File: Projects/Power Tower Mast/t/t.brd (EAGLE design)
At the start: 16.6 x 21.5 mm, 27 parts

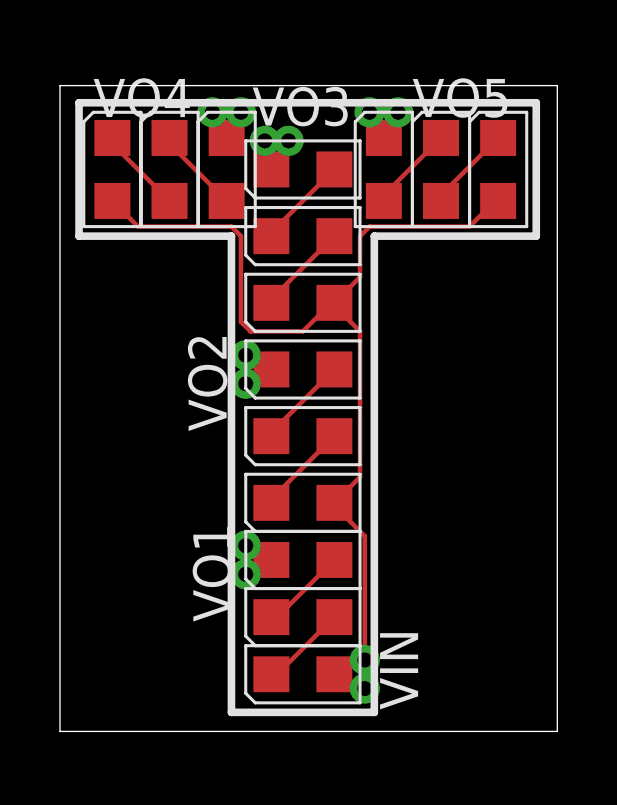
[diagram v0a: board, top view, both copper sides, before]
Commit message: fixed ratio for all letters; continued to update layouts
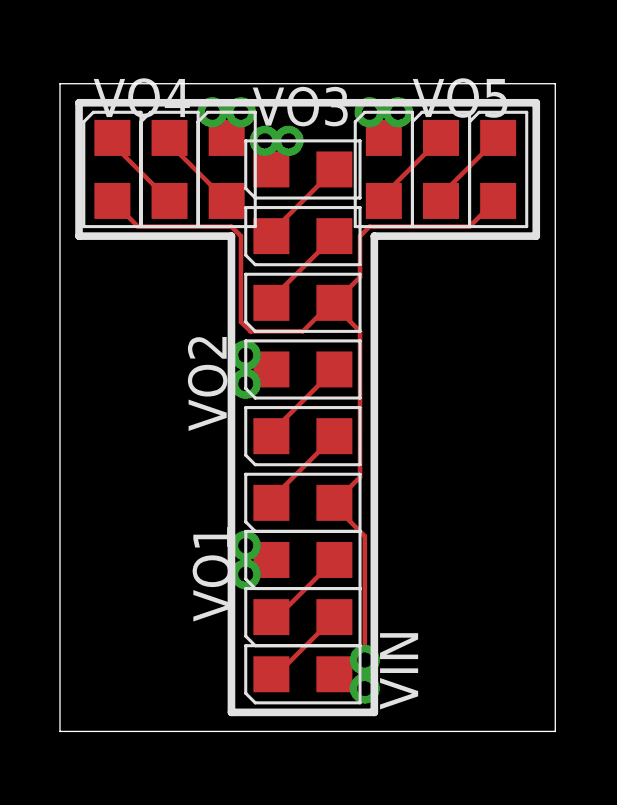
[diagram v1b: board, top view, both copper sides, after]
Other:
- board size 16.6 x 21.5 mm -> 16.5 x 21.6 mm
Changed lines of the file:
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@@
 <board>
 <plain>
-<wire x1="0" y1="0" x2="16.576646875" y2="-0.000003125" width="0" layer="20"/>
-<wire x1="16.576646875" y1="-0.000003125" x2="16.576646875" y2="21.527365625" width="0" layer="20"/>
-<wire x1="16.576646875" y1="21.527365625" x2="0" y2="21.52736875" width="0" layer="20"/>
-<wire x1="0" y1="21.52736875" x2="0" y2="0" width="0" layer="20"/>
-<text x="0.635" y="0.635" size="20.32" layer="201" font="fixed" ratio="22" distance="27">T</text>
+<wire x1="0" y1="0" x2="16.51" y2="0" width="0" layer="20"/>
+<wire x1="16.51" y1="0" x2="16.51" y2="21.59" width="0" layer="20"/>
+<wire x1="16.51" y1="21.59" x2="0" y2="21.59" width="0" layer="20"/>
+<wire x1="0" y1="21.59" x2="0" y2="0" width="0" layer="20"/>
+<text x="0.635" y="0.635" size="20.32" layer="201" font="fixed" ratio="15" distance="27">T</text>
 <wire x1="0.635" y1="20.955" x2="0.635" y2="16.51" width="0.254" layer="21"/>
 <wire x1="0.635" y1="16.51" x2="5.715" y2="16.51" width="0.254" layer="21"/>
